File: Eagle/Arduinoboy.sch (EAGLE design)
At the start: 22 parts

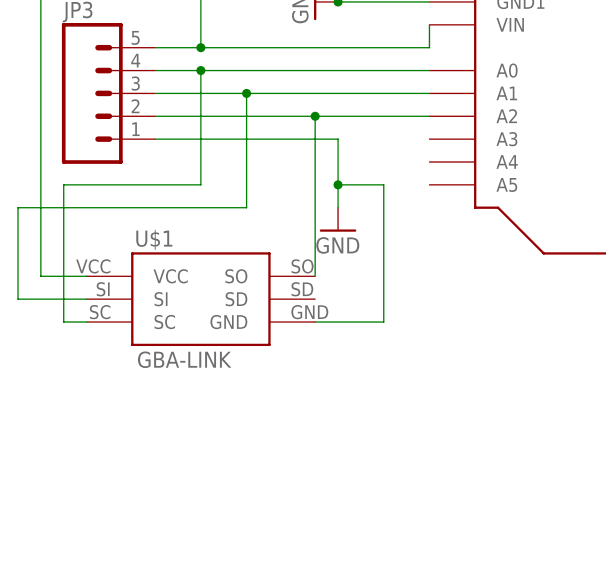
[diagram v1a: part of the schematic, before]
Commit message: Fix PCB bugs
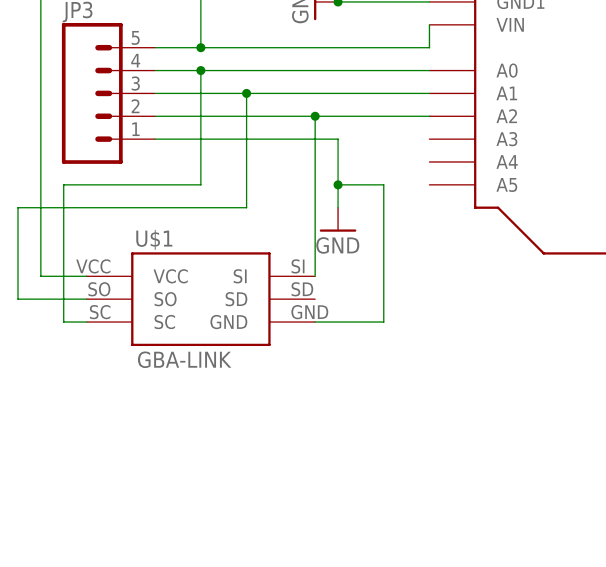
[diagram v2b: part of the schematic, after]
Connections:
- net N$22: now also U$1.SO; no longer U$1.SI
- net N$23: now also U$1.SI; no longer U$1.SO
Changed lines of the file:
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@@
 <wire x1="-40.64" y1="111.76" x2="-40.64" y2="124.46" width="0.1524" layer="91"/>
 <junction x="-40.64" y="124.46"/>
-<pinref part="U$1" gate="G$1" pin="SI"/>
+<pinref part="U$1" gate="G$1" pin="SO"/>
 </segment>
 </net>
@@
 <wire x1="-33.02" y1="104.14" x2="-33.02" y2="121.92" width="0.1524" layer="91"/>
 <junction x="-33.02" y="121.92"/>
-<pinref part="U$1" gate="G$1" pin="SO"/>
+<pinref part="U$1" gate="G$1" pin="SI"/>
 </segment>
 </net>

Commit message: Add eagle files for v1.1.0
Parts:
- removed JP1: (no value), SparkFun-Connectors:M025MM
- removed JP2: (no value), SparkFun-Connectors:M03-SCREW-5MM
- removed JP3: (no value), SparkFun-Connectors:M05SCREW
- removed U$4, U$5: MIDI_CONN_FEMALE_SUPPORT, SparkFun-Connectors:MIDI_CONN_FEMALE_SUPPORT
- added U$2, U$6: MIDI-DIN-5, MIDI by Jazz:MIDI-DIN-5
- added X1: (no value), mini_din:MINI_DIN_6
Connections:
- removed net N$22: JP3.3, U$1.SO, U$3.A1
- removed net N$23: JP3.2, U$1.SI, U$3.A2
- removed net N$24: JP3.5, U$1.VCC, U$3.VIN
- new net N$19: R1.2, U$6.4
- new net N$20: U$1.SI, U$3.A2, X1.1
- new net N$21: U$1.SO, U$3.A1
- net GND: now also U$2.2, X1.3; no longer JP2.1, JP3.1, U$4.GND
- net N$17: now also X1.5; no longer JP3.4
- net N$18: now also U$1.VCC, U$3.VIN; no longer JP1.1, R1.2, U$5.CSRC
- net N$2: now also U$6.5; no longer JP1.2, U$5.CSNK
- net N$5: now also U$2.4; no longer JP2.2, U$4.CSRC
- net N$7: now also U$2.5; no longer JP2.3, U$4.CSNK
- net VCC: now also X1.4
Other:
- moved on the sheet: R3, U$1
